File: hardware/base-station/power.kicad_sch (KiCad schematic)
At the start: 31 parts, among them U2 LM5157QRTERQ1, U4 TPS22810TDBVRQ1, U9 TPS63021DSJR

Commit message: hardware: BOM-cost pass across all four boards
Component changes from a cross-board cost review. Per-board component cost
(USD @~100qty): rocket $86.21 -> $61.39, base station $35.91 -> $29.89, with
the LoRa daughterboard and GNSS SAM-M10Q board added to the shared BOM.

Memory architecture
  - Rocket: MR25H10 MRAM deleted; the log ring moves to in-package PSRAM.
    ESP32-S3 -> ESP32-S3RH2 (2 MB quad PSRAM, no in-package flash, same land
    pattern; SPICS1/GPIO26 was already unconnected on every board).
    Persistence across boots is knowingly given up.
  - Rocket NAND F35SQB004G-WWT -> GD5F2GQ5UEYIGR: pin- and footprint-identical
    (verified against the U11 land pattern), 4 Gbit -> 2 Gbit, $11.61 -> $3.50.
    Needs the 4096 -> 2048 B page migration in firmware.
  - Base station: dedicated log flash deleted entirely. It wrote one ~183 B CSV
    row per received packet at the 2 Hz downlink (~366 B/s, and only while a
    flight is active), so 256 MB was ~204 hours of headroom. The firmware
    already falls back to the existing SPIFFS partition, so this promotes a
    tested path rather than needing new code.
  - Boot flash W25Q64JVXGIQ -> W25Q128JVSIQ on all four positions: 16 MB for
    LESS money ($3.10 -> $2.21). SCHEMATIC ONLY - the boards still need
    "Update PCB from Schematic" plus re-placement, since SOIC-8 208mil is 2.2x
    the DFN's area. The DFN's 9th (exposed) pad was a redundant GND tie; pin 4
    is GND on all four, so nothing is lost.

Power
  - LoRa + GNSS keep TPS62913 (low-noise, RF rails). The rocket briefly moved
    to it and was REVERTED to TPS62152: the TPS62913 is forced-PWM with 5 mA
    quiescent, which would have raised the pad-idle floor ~6x against the
    light-sleep work.
  - Base load switch TPS22810 -> TPS22918 (identical footprint and pin order;
    pin 3 EN/UVLO -> ON is safe because it was driven as a plain enable).
    CT cap 10 nF -> 2.2 nF to match the rocket's ramp; R8 (QOD->VOUT) deleted.
  - LoRa gains a 7.5k S-CONF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
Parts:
- removed C20: 1 uF, Capacitor_SMD:C_0402_1005Metric, symbol Device:C
- removed C22: 10 nF, Capacitor_SMD:C_0402_1005Metric, symbol Device:C
- removed L1: WE-MAPI_4020, Footprints:WE-MAPI_4020, symbol Custom:WE-MAPI_4020
- removed R8: 1 k, Resistor_SMD:R_0402_1005Metric, symbol Device:R_US
- removed U4: TPS22810TDBVRQ1, Footprints:SOT95P280X145-6N, symbol Custom:TPS22810TDBVRQ1
- added C42: 1 uF, Capacitor_SMD:C_0402_1005Metric, symbol Device:C
- added C88: 2.2 nF, Capacitor_SMD:C_0402_1005Metric, symbol Device:C
- added L8: VLS3012CX-2R2M-1, Footprints:IND_VLS3012CX-2R2M-1, symbol Custom:VLS3012CX-2R2M-1
- added U22: TPS22918DBVR, Footprints:SOT95P280X145-6N, symbol Custom:TPS22918DBVR
- C34: value 2.2 uF -> 22 uF
- C40: value 10 uF -> 22 uF
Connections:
- net GND: now also C42.2, C88.2, U22.2 (GND)
- net VCC: now also C42.1, L8.1, U22.1 (VIN)
- net at C23.1, C59.1, U9.10 (VIN_10)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: now also U22.5 (QOD), U22.6 (VOUT)
- net at C21.1, R7.2, S1.1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: now also U22.3 (ON)
- net at D2.A, U2.12 (SW), U2.13 (SW)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: now also L8.2
- new net: C88.1, U22.4 (CT)
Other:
- moved on the sheet: C21, R7, S1

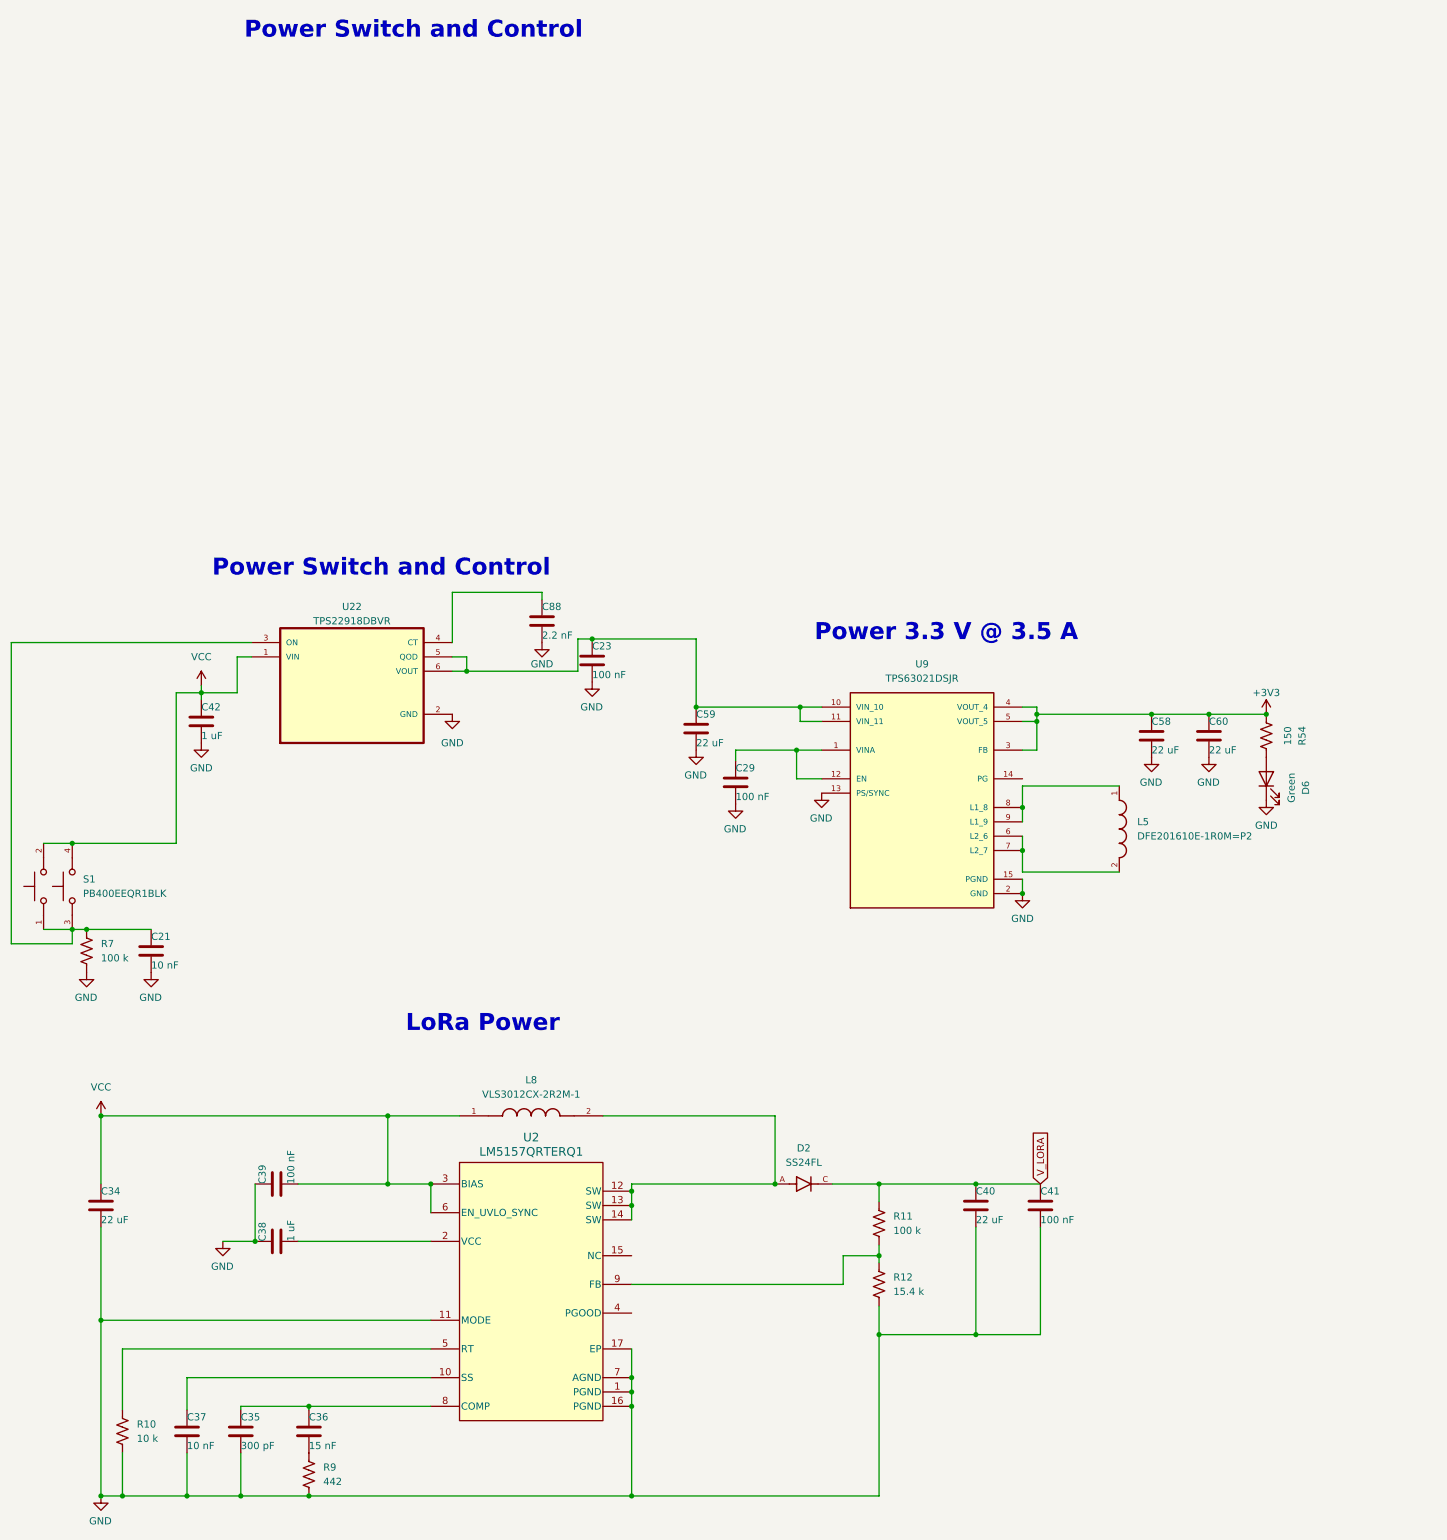
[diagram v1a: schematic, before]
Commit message: hardware: battery protection, boost swap, and a capacitor voltage audit
Base station power chain, all verified against exported netlists:

- Protection: MAX17303G+ gauge/protector and its NTMD6N02R2G FET pair
  replaced by DW01A + 2x FS8205A. The MAX17303 had no firmware driver and
  the board never had a working coulomb counter, so state of charge already
  came from the voltage curve in bs_battery_soc.h; it now reads a 1M/1M
  divider on GPIO1. The FETs move from the positive rail to the negative
  one because the DW01A has no charge pump, so board ground is now P-,
  separated from the cell's B- by the FET stack. Two FS8205A in parallel
  put the 150 mV overcurrent trip at ~4.8-6.0 A instead of ~2.4-3.0 A.
  TH1 moves onto the BQ21040's TS pin, replacing a fixed 10k that had been
  defeating thermal charge cutoff.

- V_LORA retargeted 7.49 V -> 4.95 V and LM5157QRTERQ1 -> TPS61023DRLR.
  Nothing needed 7.4 V (everything downstream is 3.3 V behind the
  TPS62913), while an RFD868x-class radio is 5 V nominal with a 6 V
  absolute maximum, so the old rail put it permanently out of reach. Being
  synchronous and internally compensated also dropped D2, C35-C38 and R10.
  Inductor stays the fleet 2.2 uH: inside TI's 0.37-2.9 uH range and the
  only value meeting their ripple-under-40%-of-average guidance at load.

- Keystone 1043P holder -> MYOUNG BH-18650-A5BJ001-2D. Terminal pitch
  72.30 vs 72.22 mm, so the battery nets did not move; BT2 is rotated 180
  degrees because this part's positive end is mirrored.

Across all four boards:

- Every crystal was mis-loaded. 32.768 kHz parts saw ~9 pF against a 6 pF
  spec and the 40 MHz saw 12.5 pF against 10 pF, both pulling slow. Moved
  to Seiko SC-32S (12.5 pF) with 22 pF load caps, and the 40 MHz caps to
  18 pF. The tolerance being paid for had been swamped several times over.

- Capacitor voltage audit, new Min V rating column in the BOM. Three parts
  were operating outside their rating on 8.4 V rails: 47 uF and 100 u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
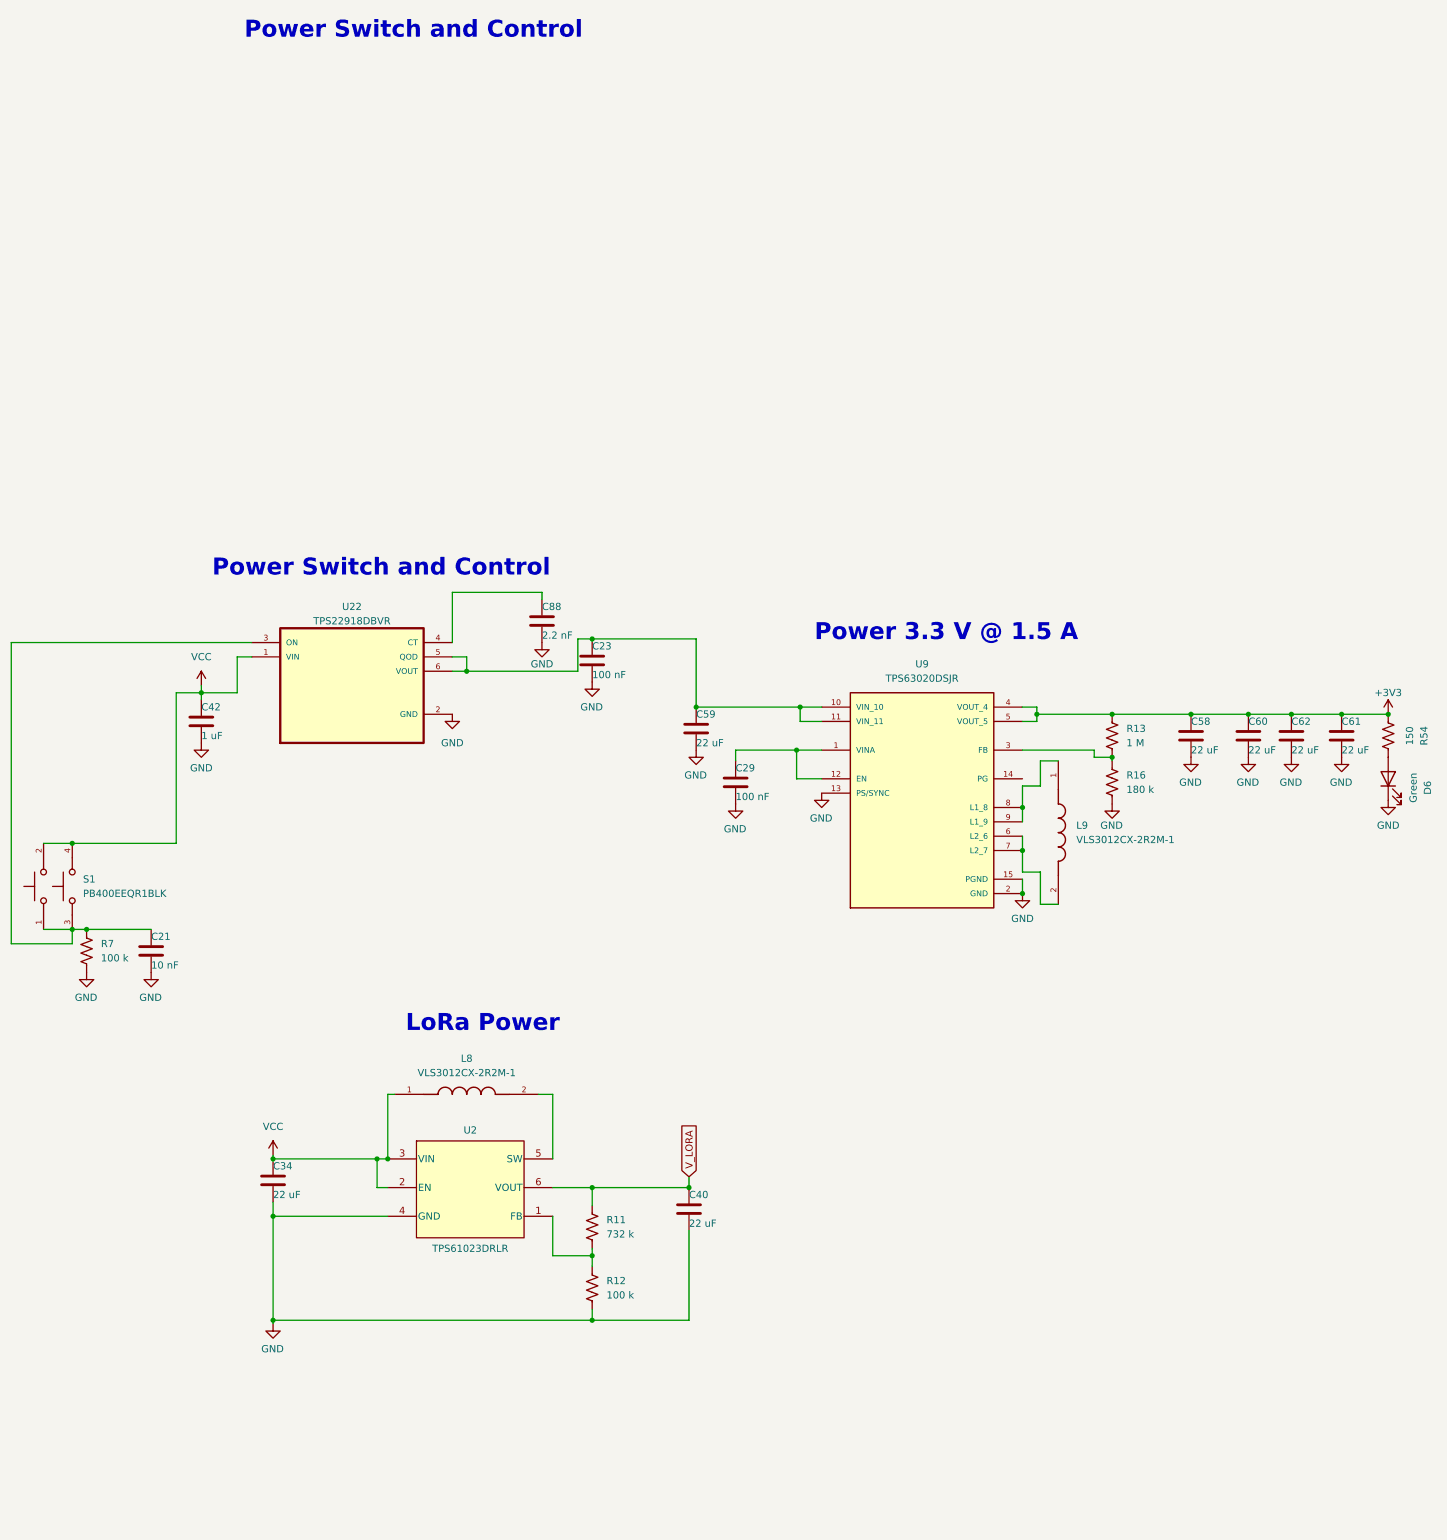
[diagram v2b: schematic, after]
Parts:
- removed C35: 300 pF, Capacitor_SMD:C_0402_1005Metric, symbol Device:C
- removed C36: 15 nF, Capacitor_SMD:C_0402_1005Metric, symbol Device:C
- removed C37: 10 nF, Capacitor_SMD:C_0402_1005Metric, symbol Device:C
- removed C38: 1 uF, Capacitor_SMD:C_0402_1005Metric, symbol Device:C
- removed C39, C41: 100 nF, Capacitor_SMD:C_0402_1005Metric, symbol Device:C
- removed D2: SS24FL, Footprints:SODFL3617X108N, symbol Custom:SS24FL
- removed L5: DFE201610E-1R0M=P2, Footprints:INDC2016X100N, symbol Custom:DFE201610E-1R0M=P2
- removed R10: 10 k, Resistor_SMD:R_0402_1005Metric, symbol Device:R_US
- removed R9: 442, Resistor_SMD:R_0402_1005Metric, symbol Device:R_US
- removed U2: LM5157QRTERQ1, RTE0016K, symbol Custom:LM5157QRTERQ1
- added C61, C62: 22 uF, Capacitor_SMD:C_0805_2012Metric, symbol Device:C
- added L9: VLS3012CX-2R2M-1, Footprints:IND_VLS3012CX-2R2M-1, symbol Custom:VLS3012CX-2R2M-1
- added R13: 1 M, Resistor_SMD:R_0402_1005Metric, symbol Device:R_US
- added R16: 180 k, Resistor_SMD:R_0402_1005Metric, symbol Device:R_US
- added U2: TPS61023DRLR, Footprints:DRL0006A, symbol Custom:TPS61023DRLR
- R11: value 100 k -> 732 k
- R12: value 15.4 k -> 100 k
- U9: value TPS63021DSJR -> TPS63020DSJR
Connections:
- net +3V3: now also C61.1, C62.1, R13.2; no longer U9.3 (FB)
- net GND: now also C61.2, C62.2, R16.1, U2.4 (GND)
- net VCC: now also U2.2 (EN), U2.3 (VIN)
- net V_LORA: now also U2.6 (VOUT)
- net at R11.1, R12.2: now also U2.1 (FB)
- net at L8.2: now also U2.5 (SW)
- net at U9.6 (L2_6), U9.7 (L2_7): now also L9.2
- net at U9.8 (L1_8), U9.9 (L1_9): now also L9.1
- new net: R13.1, R16.2, U9.3 (FB)
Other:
- note added: "Power 3.3 V @ 1.5 A"
- note removed: "Power 3.3 V @ 3.5 A"
- moved on the sheet: C34, C40, C58, C60, D6, L8, R11, R12, R54

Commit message: hardware: WIP -- 1k series R on cross-board UARTs, BS LoRa boost behind the load switch
*** Schematic-side only. Two of the three boards' layouts have not caught
    up, and the rocket-computer PCB is still mid-rework. Do not fabricate
    from this revision. ***

Three review follow-ups, all schematic:

1. Camera UART series resistors (rocket-computer, external_connections)
   R30, R32 = 1 k 0402 inserted in the camera link:
     Camera_RX  U17.61 -> R30 -> J4.3
     Camera_TX  U17.60 -> R32 -> J4.4
   Mitigation for the V9 review's H6: the peripheral ports are ground-side
   switched while their supply pins stay live, so an off-state peripheral
   floats toward VBATT and injects into P4 GPIOs through the signal lines.
   H6's recommendation was ">= 1 k series resistors or bus switches on
   every cross-connector signal". PCB: R30/R32 ARE placed, F.Cu
   (97.31,156.38) and (97.31,158.38).

2. GNSS UART series resistors (gnss-sam10m8-18mm-hv)
   R7, R8 = 1 k 0402, same pattern:
     GNSS_RX  U1.14 -> R7 -> J3.1
     GNSS_TX  U1.13 -> R8 -> J3.2
   PCB: R7/R8 are NOT placed. Needs Update PCB from Schematic.

3. LoRa boost moved behind the load switch (base-station, power)
   U2 (TPS61023, the V_LORA boost) VIN+EN and its inductor L8 and C34 move
   from VCC to the new V_SWITCH net, downstream of U22 (TPS22918).
   Net-(U22-QOD) is renamed V_SWITCH and now carries
   {C23, C34, C59, L8.1, U2.2, U2.3, U22.5, U22.6, U9.10, U9.11}.
   This closes the LoRa V3 review's finding 14: previously the base
   station could not power-cycle the radio daughterboard, because the
   boost's EN was tied to VCC and a boost passes VIN through its body
   diode regardless. Switching the boost input makes a real power cycle
   possible. PCB: not updated -- the net change needs re-routing.

DRC as merged (kicad-cli, severity-error, with parity):
  gnss-sam10m8   0 violations, 0 unconnected  -- but R7/R8 absent from copper
  base-station  10 violations (all malformed_courtyard on U15), 0 un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
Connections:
- net VCC: no longer C34.1, L8.1, U2.2 (EN), U2.3 (VIN)
- net V_SWITCH: now reaches C23.1, C59.1, U22.5 (QOD), U22.6 (VOUT), U9.10 (VIN_10), U9.11 (VIN_11)
- net V_SWITCH: now also C34.1, L8.1, U2.2 (EN), U2.3 (VIN)
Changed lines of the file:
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@@
 		)
 	)
+	(global_label "V_SWITCH"
+		(shape input)
+		(at 60.96 122.555 90)
+		(fields_autoplaced yes)
+		(effects
+			(font
+				(size 1.27 1.27)
+			)
+			(justify left)
+		)
+		(property "Intersheetrefs" "${INTERSHEET_REFS}"
+			(at 60.96 110.6798 90)
+			(hide yes)
+			(show_name no)
+			(do_not_autoplace no)
+			(effects
+				(font
+					(size 1.27 1.27)
+				)
+				(justify left)
+			)
+		)
+	)
+	(global_label "V_SWITCH"
+		(shape input)
+		(at 135.89 31.115 90)
+		(fields_autoplaced yes)
+		(effects
+			(font
+				(size 1.27 1.27)
+			)
+			(justify left)
+		)
+		(property "Intersheetrefs" "${INTERSHEET_REFS}"
+			(at 135.89 19.2398 90)
+			(hide yes)
+			(show_name no)
+			(do_not_autoplace no)
+			(effects
+				(font
+					(size 1.27 1.27)
+				)
+				(justify left)
+			)
+		)
+	)
 	(global_label "V_LORA"
 		(shape input)
@@
 					(unit 1)
 				)
-			)
-		)
-	)
-	(symbol
-		(lib_id "power:VCC")
-		(at 60.96 122.555 0)
-		(unit 1)
-		(body_style 1)
-		(exclude_from_sim no)
-		(in_bom yes)
-		(on_board yes)
-		(in_pos_files yes)
-		(dnp no)
-		(fields_autoplaced yes)
-		(property "Reference" "#PWR049"
-			(at 60.96 126.365 0)
-			(hide yes)
-			(show_name no)
-			(do_not_autoplace no)
-			(effects
-				(font
-					(size 1.27 1.27)
-				)
-			)
-		)
-		(property "Value" "VCC"
-			(at 60.96 117.475 0)
-			(show_name no)
-			(do_not_autoplace no)
-			(effects
-				(font
-					(size 1.27 1.27)
-				)
-			)
-		)
-		(property "Footprint" ""
-			(at 60.96 122.555 0)
-			(hide yes)
-			(show_name no)
-			(do_not_autoplace no)
-			(effects
-				(font
-					(size 1.27 1.27)
-				)
-			)
-		)
-		(property "Datasheet" ""
-			(at 60.96 122.555 0)
-			(hide yes)
-			(show_name no)
-			(do_not_autoplace no)
-			(effects
-				(font
-					(size 1.27 1.27)
-				)
-			)
-		)
-		(property "Description" "Power symbol creates a global label with name \"VCC\""
-			(at 60.96 122.555 0)
-			(hide yes)
-			(show_name no)
-			(do_not_autoplace no)
-			(effects
-				(font
-					(size 1.27 1.27)
-				)
-			)
-		)
-		(pin "1"
-		)
-		(instances
-			(project "base-station"
-				(path "/d2421514-d142-4c71-ac69-48d30c1a771f/a2c0dd5a-afba-424d-8751-54eedd450b6c"
-					(reference "#PWR049")
-					(unit 1)
-				)
